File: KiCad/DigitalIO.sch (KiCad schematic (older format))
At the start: 116 parts, among them J201 DI1, J202 DI2, J203 DI3, J204 DI4, J205 DI5, J206 DI6, J207 DI7, J208 DI8, J209 DO1/2, J210 DO3/4, J211 DO5/6, J212 DO7/8, J213 GND, J214 GND, J215 GND, J216 GND, Q201 ZXTN25050DFHTA, Q202 ZXTN25050DFHTA, Q203 ZXTN25050DFHTA, Q204 ZXTN25050DFHTA, Q205 ZXTN25050DFHTA, Q206 ZXTN25050DFHTA, Q207 ZXTN25050DFHTA, Q208 ZXTN25050DFHTA, U201 LTV-354T, U202 LTV-354T, U203 LTV-354T, U204 LTV-354T, U205 LTV-354T, U206 LTV-354T, U207 LTV-354T, U208 LTV-354T, U209 MCP23017

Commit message: Remade layout
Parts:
- D215, D216, D217, D218, D219, D220, D223, D224: footprint Diodes_THT:D_DO-41_SOD81_P5.08mm_Vertical_KathodeUp -> Diodes_THT:D_DO-41_SOD81_P2.54mm_Vertical_KathodeUp
- renumbered R243 to R225, R244 to R226, R245 to R227, R246 to R228, R247 to R229, R248 to R230, R249 to R231, R250 to R232, R225 to R233, R226 to R234, R227 to R235, R228 to R236, R229 to R237, R230 to R238, R231 to R239, R232 to R240, R233 to R241, R234 to R242, R235 to R243, R236 to R244, R237 to R245, R238 to R246, R239 to R247, R240 to R248, R241 to R249, R242 to R250
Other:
- moved on the sheet: J215

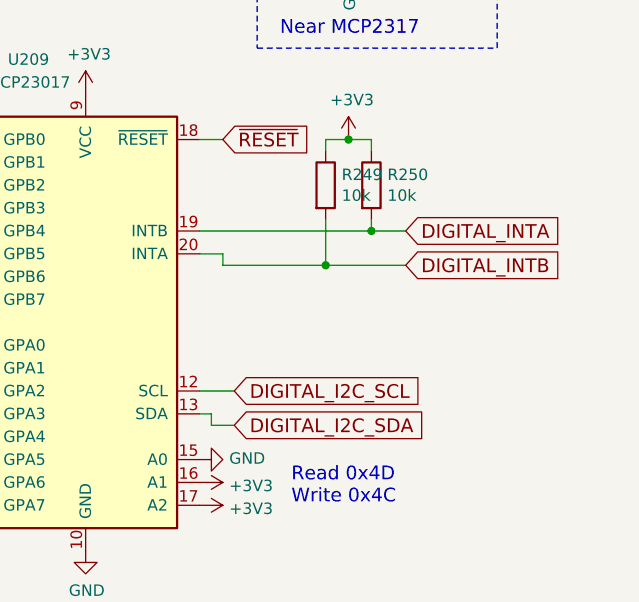
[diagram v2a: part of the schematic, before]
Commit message: Save with sensor inputs using digital potentiometer
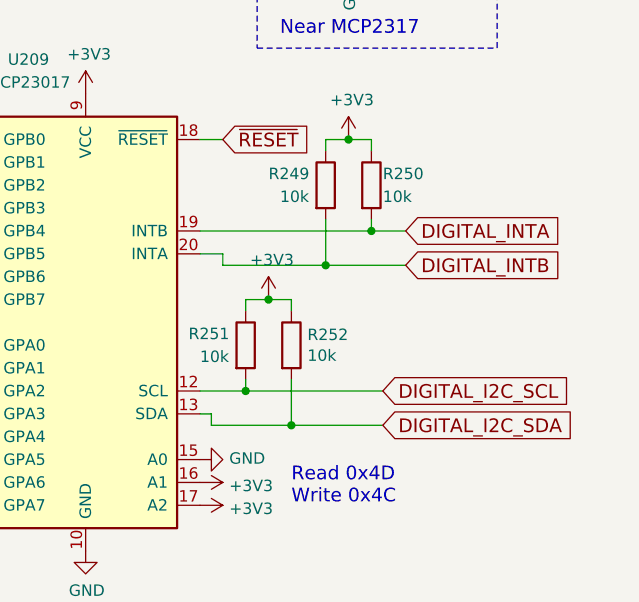
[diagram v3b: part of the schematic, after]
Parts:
- added R251, R252: 10k, Resistors_SMD:R_0805, symbol R
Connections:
- net +3V3: now also R251.1, R252.1
- net DIGITAL_I2C_SCL: now also R251.2
- net DIGITAL_I2C_SDA: now also R252.2

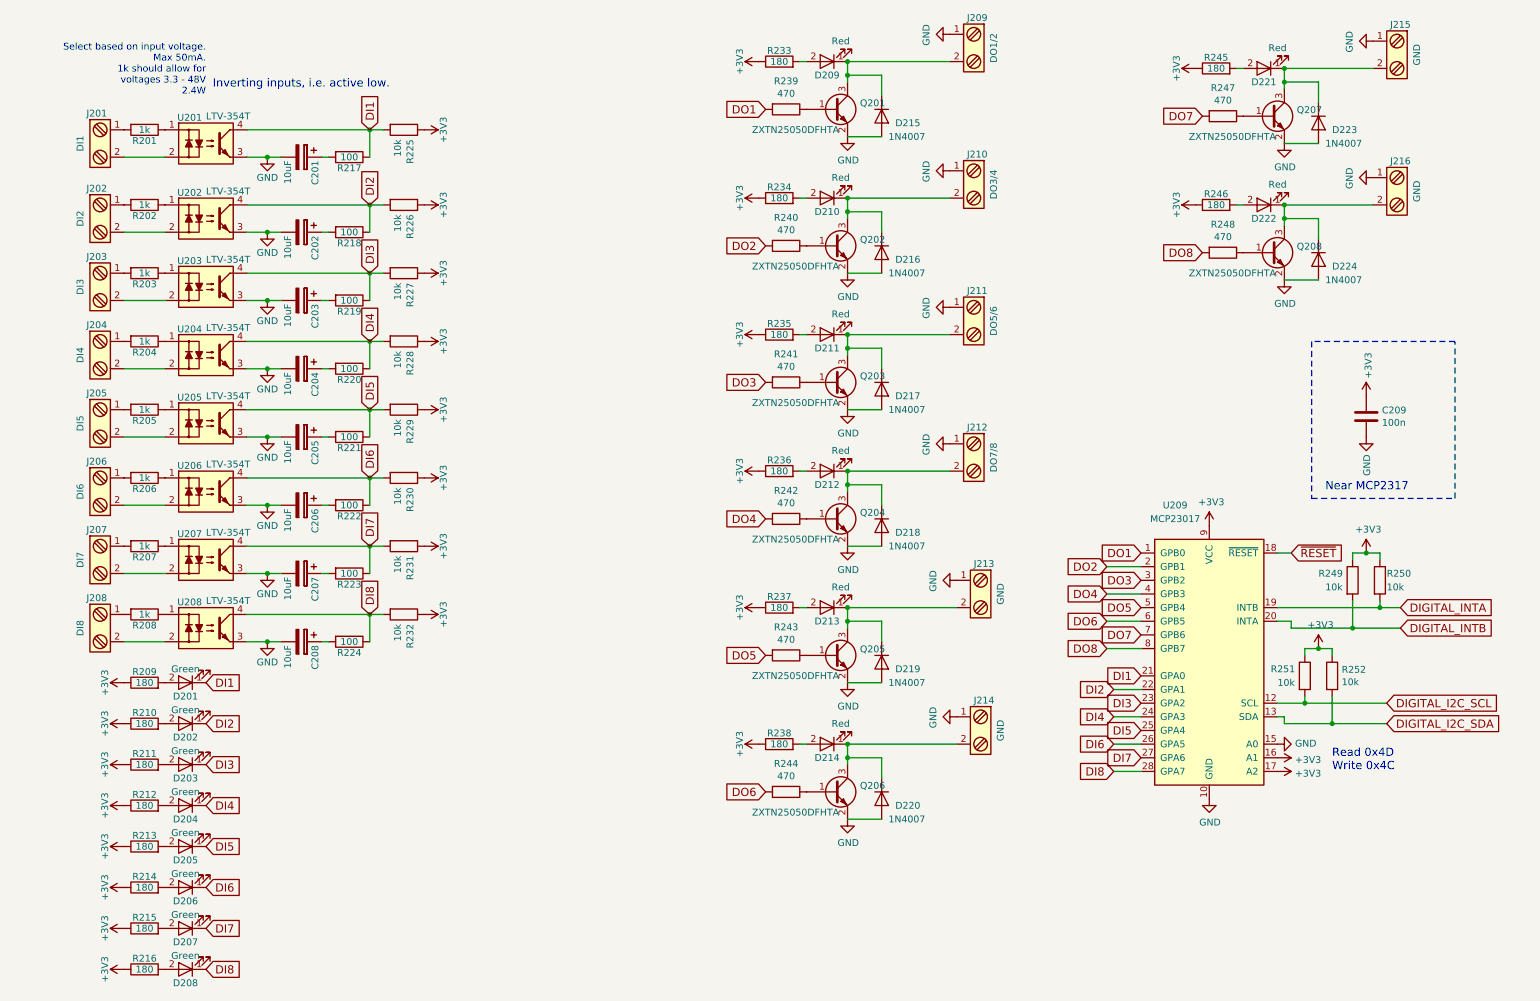
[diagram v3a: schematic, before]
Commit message: Inputs reworked. New terminals
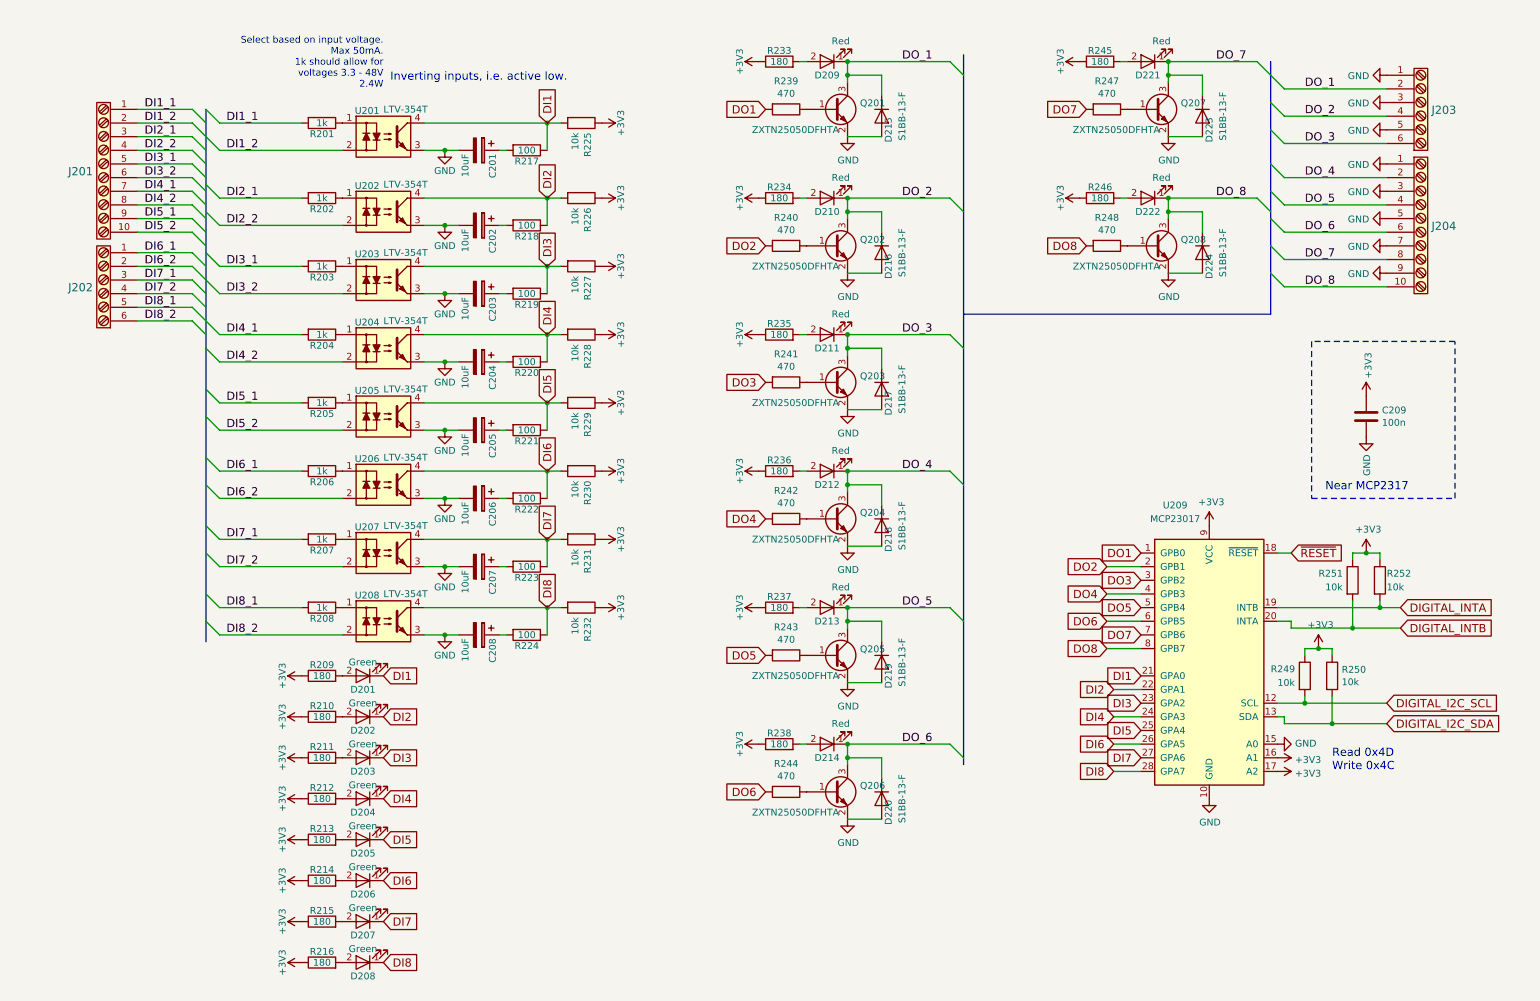
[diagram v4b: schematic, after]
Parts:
- removed J201: DI1, Connectors_Terminal_Blocks:TerminalBlock_Pheonix_MPT-2.54mm_2pol, symbol Screw_Terminal_1x02
- removed J202: DI2, Connectors_Terminal_Blocks:TerminalBlock_Pheonix_MPT-2.54mm_2pol, symbol Screw_Terminal_1x02
- removed J203: DI3, Connectors_Terminal_Blocks:TerminalBlock_Pheonix_MPT-2.54mm_2pol, symbol Screw_Terminal_1x02
- removed J204: DI4, Connectors_Terminal_Blocks:TerminalBlock_Pheonix_MPT-2.54mm_2pol, symbol Screw_Terminal_1x02
- removed J205: DI5, Connectors_Terminal_Blocks:TerminalBlock_Pheonix_MPT-2.54mm_2pol, symbol Screw_Terminal_1x02
- removed J206: DI6, Connectors_Terminal_Blocks:TerminalBlock_Pheonix_MPT-2.54mm_2pol, symbol Screw_Terminal_1x02
- removed J207: DI7, Connectors_Terminal_Blocks:TerminalBlock_Pheonix_MPT-2.54mm_2pol, symbol Screw_Terminal_1x02
- removed J208: DI8, Connectors_Terminal_Blocks:TerminalBlock_Pheonix_MPT-2.54mm_2pol, symbol Screw_Terminal_1x02
- removed J209: DO1/2, Connectors_Terminal_Blocks:TerminalBlock_Pheonix_MPT-2.54mm_2pol, symbol Screw_Terminal_1x02
- removed J210: DO3/4, Connectors_Terminal_Blocks:TerminalBlock_Pheonix_MPT-2.54mm_2pol, symbol Screw_Terminal_1x02
- removed J211: DO5/6, Connectors_Terminal_Blocks:TerminalBlock_Pheonix_MPT-2.54mm_2pol, symbol Screw_Terminal_1x02
- removed J212: DO7/8, Connectors_Terminal_Blocks:TerminalBlock_Pheonix_MPT-2.54mm_2pol, symbol Screw_Terminal_1x02
- removed J213, J214, J215, J216: GND, Connectors_Terminal_Blocks:TerminalBlock_Pheonix_MPT-2.54mm_2pol, symbol Screw_Terminal_1x02
- added J201, J204: TE_Connectivity_1-282834-0, TE_Connectivity:TE_Connectivity_1-282834-0, symbol TE_Connectivity_1-282834-0
- added J202, J203: TE_Connectivity_282834-6, TE_Connectivity:TE_Connectivity_282834-6, symbol TE_Connectivity_282834-6
- D215, D216, D217, D218, D219, D220, D223, D224: value 1N4007 -> S1BB-13-F; footprint Diodes_THT:D_DO-41_SOD81_P2.54mm_Vertical_KathodeUp -> Diodes_SMD:D_SMB
- renumbered R251 to R249, R252 to R250, R249 to R251, R250 to R252
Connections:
- net GND: now also J203.1, J203.3, J203.5, J204.1, J204.3, J204.5, J204.7, J204.9
- net DI8_2: now reaches U208.2
- net DI8_2: now also J202.6
- net DI8_1: now reaches R208.2
- net DI8_1: now also J202.5
- net DI7_2: now reaches U207.2
- net DI7_2: now also J202.4
- net DI7_1: now reaches R207.2
- net DI7_1: now also J202.3
- net DI6_2: now reaches U206.2
- net DI6_2: now also J202.2
- net DI6_1: now reaches R206.2
- net DI6_1: now also J202.1
- net DI5_2: now reaches U205.2
- net DI5_2: now also J201.10
- net DI5_1: now reaches R205.2
- net DI5_1: now also J201.9
- net DI4_2: now reaches U204.2
- net DI4_2: now also J201.8
- net DI4_1: now reaches R204.2
- net DI4_1: now also J201.7
- net DI3_2: now reaches U203.2
- net DI3_2: now also J201.6
- net DI3_1: now reaches R203.2
- net DI3_1: now also J201.5
- net DI2_2: now reaches U202.2
- net DI2_2: now also J201.4
- net DI2_1: now reaches R202.2
- net DI2_1: now also J201.3
- net DI1_1: now reaches R201.2
- net DI1_1: now also J201.1
- net DI1_2: now reaches U201.2
- net DI1_2: now also J201.2
- net DO_1: now reaches D209.1 (K), D215.1 (K), Q201.3 (C)
- net DO_1: now also J203.2
- net DO_2: now reaches D210.1 (K), D216.1 (K), Q202.3 (C)
- net DO_2: now also J203.4
- net DO_3: now reaches D211.1 (K), D217.1 (K), Q203.3 (C)
- net DO_3: now also J203.6
- net DO_4: now reaches D212.1 (K), D218.1 (K), Q204.3 (C)
- net DO_4: now also J204.2
- net DO_5: now reaches D213.1 (K), D219.1 (K), Q205.3 (C)
- net DO_5: now also J204.4
- net DO_6: now reaches D214.1 (K), D220.1 (K), Q206.3 (C)
- net DO_6: now also J204.6
- net DO_7: now reaches D221.1 (K), D223.1 (K), Q207.3 (C)
- net DO_7: now also J204.8
- net DO_8: now reaches D222.1 (K), D224.1 (K), Q208.3 (C)
- net DO_8: now also J204.10
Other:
- moved on the sheet: C201, C202, C203, C204, C205, C206, C207, C208, D201, D202, D203, D204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

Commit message: Halfway through routing - need better layout to prevent rats nest
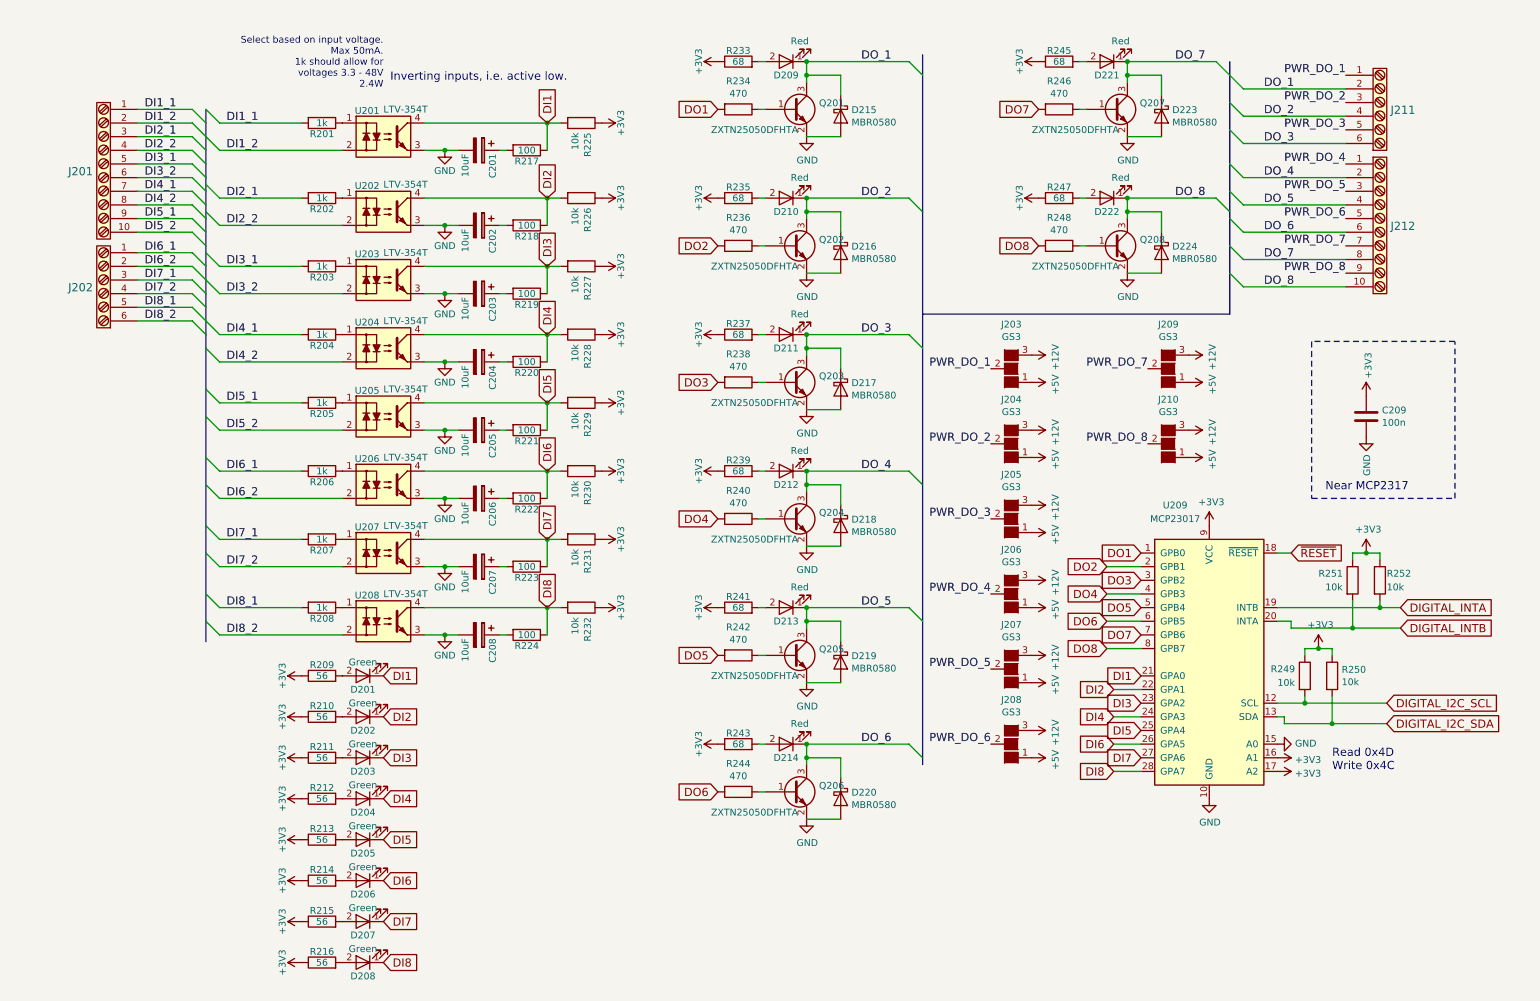
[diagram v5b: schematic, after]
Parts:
- removed D215, D216, D217, D218, D219, D220, D223, D224: S1BB-13-F, Diodes_SMD:D_SMB, symbol 1N4007
- removed R234, R236, R238, R246: 180, Resistors_SMD:R_0805, symbol R
- added D215, D216, D217, D218, D219, D220, D223, D224: MBR0580, Diodes_SMD:D_SOD-123, symbol MBR0580
- added J203, J204, J205, J206, J207, J208, J209, J210: GS3, Connectors:GS3, symbol GS3
- added R239, R241, R243, R247: 68, Resistors_SMD:R_0805, symbol R
- C201, C202, C203, C204, C205, C206, C207, C208: footprint Capacitors_SMD:C_0805 -> Capacitors_SMD:CP_Elec_5x4.5
- R209, R210, R211, R212, R213, R214, R215, R216: value 180 -> 56
- R233, R235, R237, R245: value 180 -> 68
- renumbered J203 to J211, J204 to J212, R239 to R234, R240 to R236, R241 to R238, R242 to R240, R243 to R242, R247 to R246
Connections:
- net +3V3: now also R239.1, R241.1, R243.1, R247.1
- net DO_1: now also D215.1 (K)
- net DO_2: now also D216.1 (K)
- net DO_3: now also D217.1 (K)
- net DO_4: now also D218.1 (K)
- net DO_5: now also D219.1 (K)
- net DO_6: now also D220.1 (K)
- net DO_7: now also D223.1 (K)
- net DO_8: now also D224.1 (K)
- net GND: now also D215.2 (A), D216.2 (A), D217.2 (A), D218.2 (A), D219.2 (A), D220.2 (A), D223.2 (A), D224.2 (A); no longer J211.1, J211.3, J211.5, J212.1, J212.3, J212.5, J212.7, J212.9
- net at D214.2 (A): now also R243.2
- net at D213.2 (A): now also R241.2; no longer R237.2
- net at D212.2 (A): now also R239.2
- net at D211.2 (A): now also R237.2; no longer R235.2
- net at D210.2 (A): now also R235.2
- net at D222.2 (A): now also R247.2
- new net +12V: J203.3 (G3), J204.3 (G3), J205.3 (G3), J206.3 (G3), J207.3 (G3), J208.3 (G3), J209.3 (G3), J210.3 (G3)
- new net +5V: J203.1 (G1), J204.1 (G1), J205.1 (G1), J206.1 (G1), J207.1 (G1), J208.1 (G1), J209.1 (G1), J210.1 (G1)
- new net PWR_DO_1: J203.2 (G2), J211.1
- new net PWR_DO_2: J204.2 (G2), J211.3
- new net PWR_DO_3: J205.2 (G2), J211.5
- new net PWR_DO_4: J206.2 (G2), J212.1
- new net PWR_DO_5: J207.2 (G2), J212.3
- new net PWR_DO_6: J208.2 (G2), J212.5
- new net PWR_DO_7: J209.2 (G2), J212.7
- new net PWR_DO_8: J210.2 (G2), J212.9
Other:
- moved on the sheet: D209, D210, D211, D212, D213, D214, D221, D222, J211, J212, Q201, Q202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
